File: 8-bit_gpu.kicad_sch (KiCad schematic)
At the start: 12 parts, among them J1 DE15_Pins_HighDensity_Mountin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, U1 74LS163, U10 27C512, U2 74LS163, U3 74LS163, U4 CD4033B, U5 74HC245, U6 74LS573, U7 74HC595, U8 74HC595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

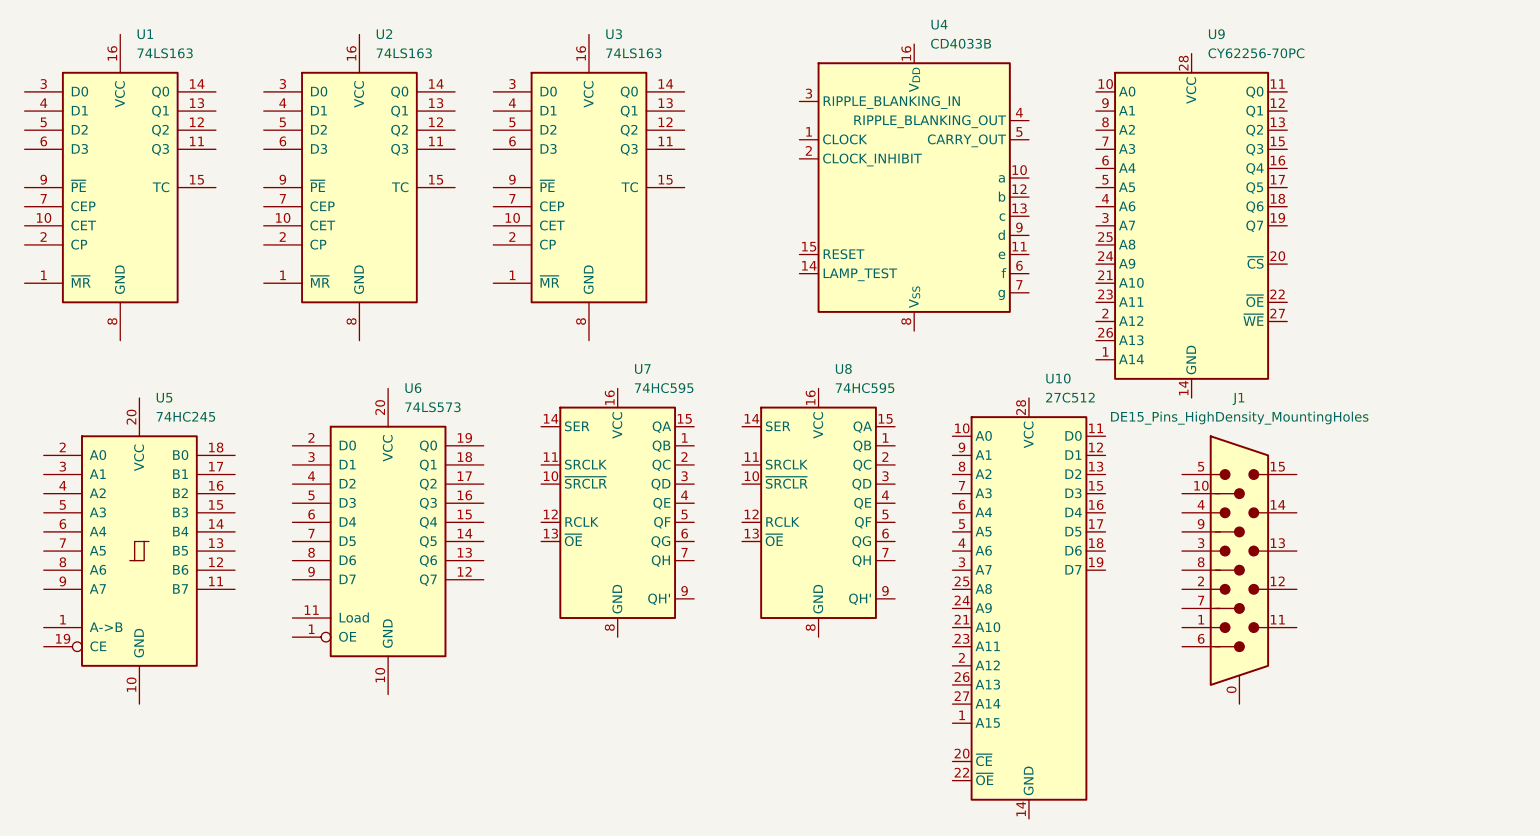
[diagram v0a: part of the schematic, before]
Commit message: Switched from ChatGPT's idea to using a pre exsiting schematic to start with
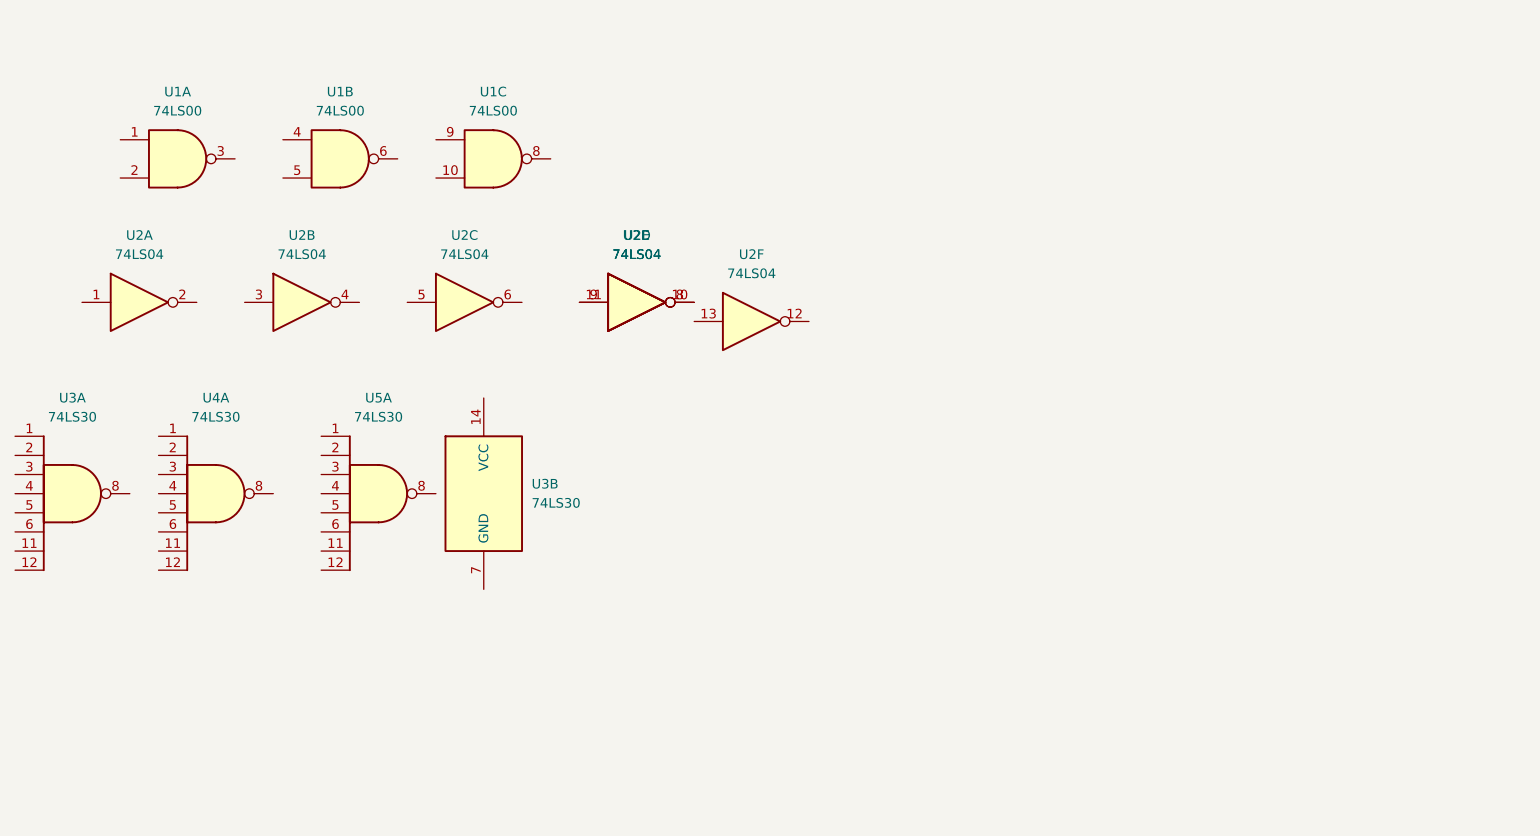
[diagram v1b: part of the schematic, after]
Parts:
- removed J1: DE15_Pins_HighDensity_MountingHoles, Connector_Dsub:DSUB-15-HD_Pins_Horizontal_P2.29x2.54mm_EdgePinOffset8.35mm_Housed_MountingHolesOffset10.89mm, symbol Connector:DE15_Pins_HighDensity_MountingHoles
- removed U1: 74LS163, Package_DIP:DIP-16_W7.62mm, symbol 74xx:74LS163
- removed U10: 27C512, Package_DIP:DIP-28_W15.24mm, symbol Memory_EPROM:27C512
- removed U2, U3: 74LS163, symbol 74xx:74LS163
- removed U4: CD4033B, Package_DIP:DIP-16_W7.62mm, symbol 4xxx:CD4033B
- removed U5: 74HC245, symbol 74xx:74HC245
- removed U6: 74LS573, symbol 74xx:74LS573
- removed U7, U8: 74HC595, symbol 74xx:74HC595
- removed U9: CY62256-70PC, Package_DIP:DIP-28_W15.24mm, symbol Memory_RAM:CY62256-70PC
- added U1: 74LS00, symbol 74xx:74LS00
- added U2: 74LS04, symbol 74xx:74LS04
- added U3, U4, U5: 74LS30, symbol 74xx:74LS30
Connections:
- new net: U2.10, U2.8
- new net: U2.11, U2.9

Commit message: Hopeing to fix issue with not being able to push
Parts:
- removed U3, U4, U5: 74LS30, symbol 74xx:74LS30
- added D1, D10, D2, D3, D4, D5, D6, D7, D8, D9: LED, symbol Device:LED
- added J1: DE15_Pins_HighDensity_MountingHoles, symbol Connector:DE15_Pins_HighDensity_MountingHoles
- added U10, U11, U12, U13, U4, U5, U6, U7, U8, U9: 74LS30, symbol 74xx:74LS30
- added U14, U18, U19, U20, U21, U3: 74LS161, symbol 74xx:74LS161
- added U15, U16, U17: 74LS04, symbol 74xx:74LS04
- added unit 7 of U2
- added U22: 28C256, symbol Memory_EEPROM:28C256
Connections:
- net at U2.10: no longer U2.8
- net at U2.11: no longer U2.9

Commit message: revert to previus version.
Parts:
- added unit 4 of U1
- added unit 5 of U1
- added U23, U24: 74LS00, symbol 74xx:74LS00
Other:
- moved on the sheet: U22

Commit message: Made the full schematic for the horazontal blanking circit.
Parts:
- removed U1: 74LS00, symbol 74xx:74LS00
- removed U15, U2: 74LS04, symbol 74xx:74LS04
- removed U18, U19, U3: 74LS161, symbol 74xx:74LS161
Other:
- added sheet HSync (H-Sync.kicad_sch)
- moved on the sheet: D1, D10, D3, D4, D5, D6, D7, D8, D9

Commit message: Set up schematic for Vertical Sync circit.
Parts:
- removed U10, U11, U12, U13, U4, U5, U6, U7, U8, U9: 74LS30, symbol 74xx:74LS30
- removed U14, U20, U21: 74LS161, symbol 74xx:74LS161
- removed U16, U17: 74LS04, symbol 74xx:74LS04
- removed U23: 74LS00, symbol 74xx:74LS00
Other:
- added sheet VSync (VSync.kicad_sch)
- sheet HSync ports: added CLK; removed none
- title: 8-Bit GPU -> Custom GPU
